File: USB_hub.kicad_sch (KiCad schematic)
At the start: 0 parts

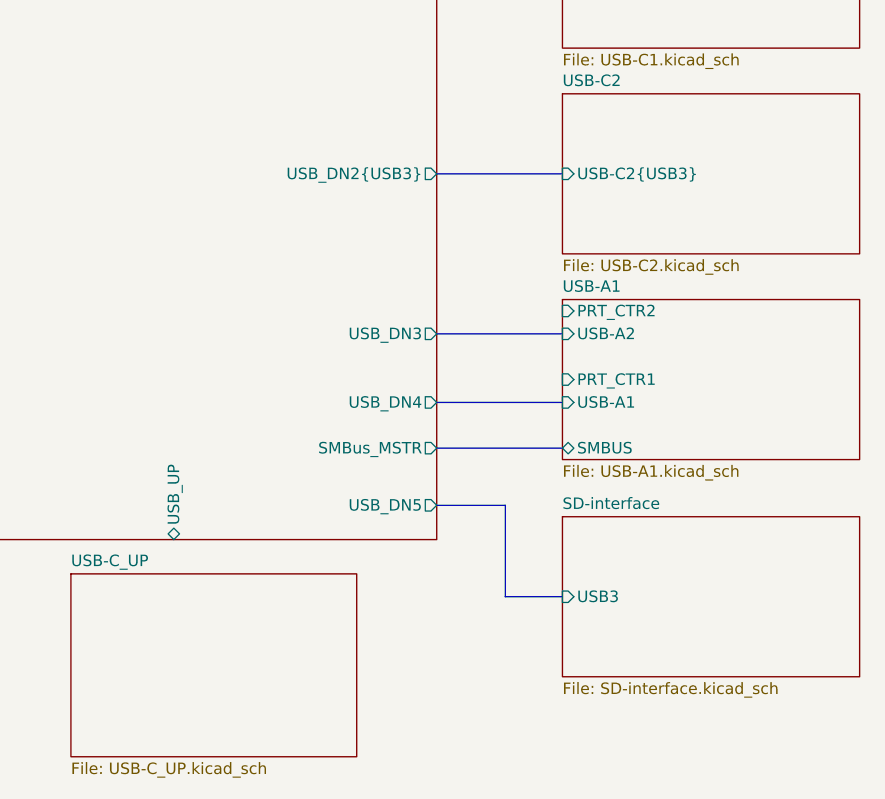
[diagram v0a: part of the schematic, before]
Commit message: labels naming fixes, USB Type E connector added
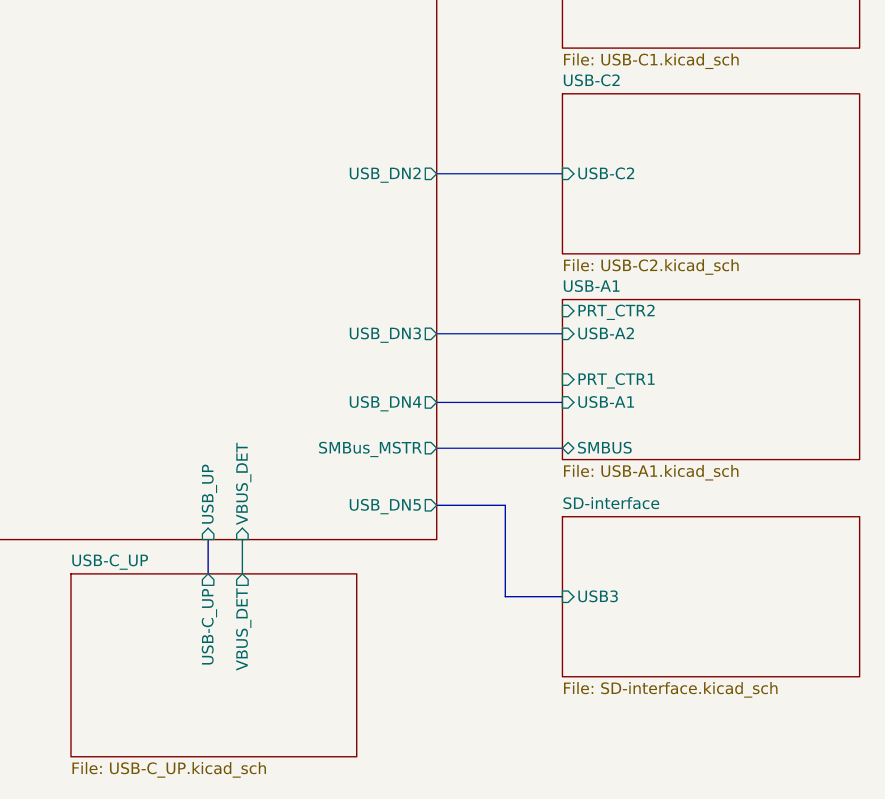
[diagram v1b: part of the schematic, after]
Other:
- sheet USB-C2 ports: added USB-C2; removed USB-C2{USB3}
- sheet USB-C_UP ports: added USB-C_UP, VBUS_DET; removed none
- sheet USB7206C ports: added USB_DN2, VBUS_DET; removed USB_DN2{USB3}
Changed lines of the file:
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@@
+		)
+	)
+	(wire
+		(pts
+			(xy 248.92 92.71) (xy 248.92 96.52)
+		)
+		(stroke
+			(width 0)
+			(type default)
 		)
 	)
@@
 		(pts
 			(xy 270.51 82.55) (xy 284.48 82.55)
+		)
+		(stroke
+			(width 0)
+			(type default)
+		)
+	)
+	(bus
+		(pts
+			(xy 245.11 92.71) (xy 245.11 96.52)
 		)
 		(stroke
@@
 			)
 		)
-		(pin "USB-C2{USB3}" input
+		(pin "USB-C2" input
 			(at 284.48 52.07 180)
 			(effects
@@
 			)
 		)
+		(pin "VBUS_DET" output
+			(at 248.92 96.52 90)
+			(effects
+				(font
+					(size 1.27 1.27)
+				)
+				(justify right)
+			)
+		)
+		(pin "USB-C_UP" output
+			(at 245.11 96.52 90)
+			(effects
+				(font
+					(size 1.27 1.27)
+				)
+				(justify right)
+			)
+		)
 		(instances
 			(project "USB_hub"
@@
 			)
 		)
-		(pin "USB_UP" bidirectional
-			(at 241.3 92.71 270)
-			(effects
-				(font
-					(size 1.27 1.27)
-				)
-				(justify left)
-			)
-		)
 		(pin "USB_DN3" output
 			(at 270.51 69.85 0)
@@
 			)
 		)
-		(pin "USB_DN2{USB3}" output
+		(pin "USB_UP" input
+			(at 245.11 92.71 270)
+			(effects
+				(font
+					(size 1.27 1.27)
+				)
+				(justify left)
+			)
+		)
+		(pin "USB_DN2" output
 			(at 270.51 52.07 0)
 			(effects
@@
 			)
 		)
+		(pin "VBUS_DET" input
+			(at 248.92 92.71 270)
+			(effects
+				(font
+					(size 1.27 1.27)
+				)
+				(justify left)
+			)
+		)

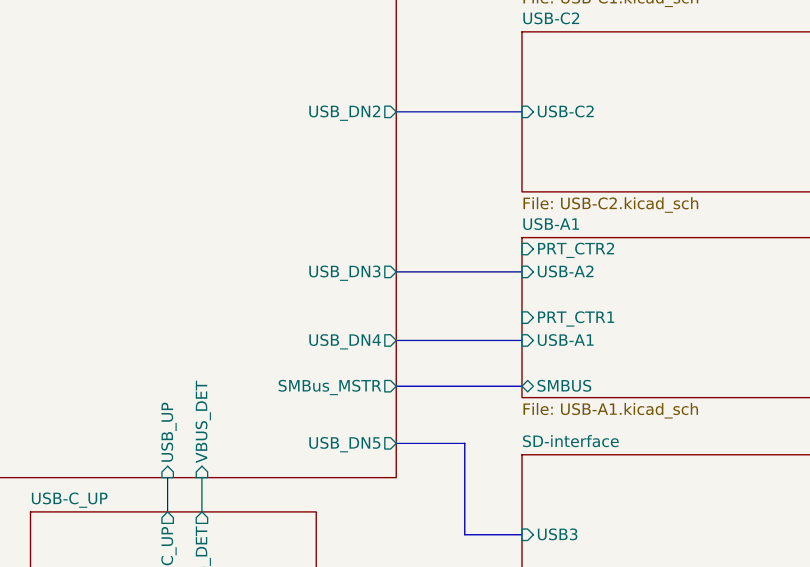
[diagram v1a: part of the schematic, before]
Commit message: Port Power Control added to USB7206C schematics
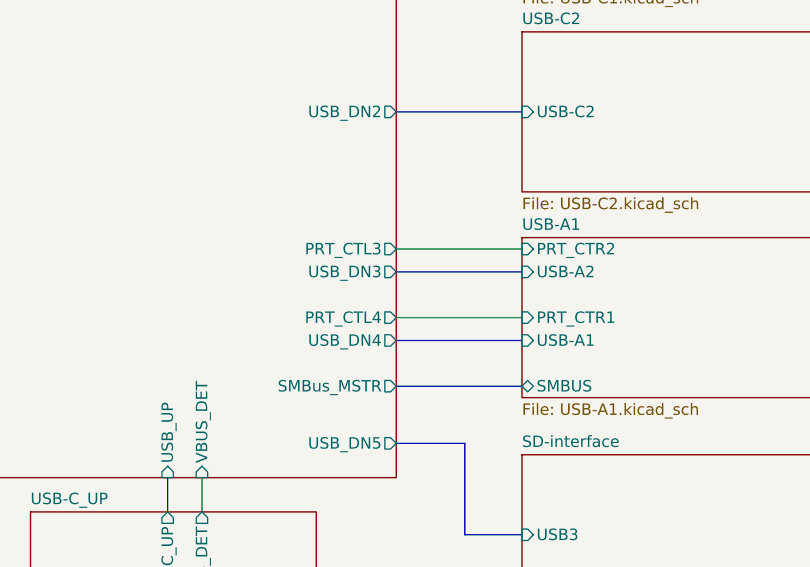
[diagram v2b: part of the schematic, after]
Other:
- sheet USB7206C ports: added PRT_CTL3, PRT_CTL4; removed none
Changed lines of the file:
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@@
+		)
+	)
+	(wire
+		(pts
+			(xy 270.51 74.93) (xy 284.48 74.93)
+		)
+		(stroke
+			(width 0)
+			(type default)
 		)
 	)
@@
 		(pts
 			(xy 270.51 29.21) (xy 284.48 29.21)
+		)
+		(stroke
+			(width 0)
+			(type default)
+		)
+	)
+	(wire
+		(pts
+			(xy 270.51 67.31) (xy 284.48 67.31)
 		)
 		(stroke
@@
 			)
 		)
+		(pin "PRT_CTL4" output
+			(at 270.51 74.93 0)
+			(effects
+				(font
+					(size 1.27 1.27)
+				)
+				(justify right)
+			)
+		)
+		(pin "PRT_CTL3" output
+			(at 270.51 67.31 0)
+			(effects
+				(font
+					(size 1.27 1.27)
+				)
+				(justify right)
+			)
+		)

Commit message: TPS25762 EEPROM connector added
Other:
- title: (none) -> USB Hub
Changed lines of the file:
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@@
 	(generator_version "9.0")
 	(paper "A3")
+	(title_block
+		(title "USB Hub")
+	)
 	(text "these connections may change for better routing "
 		(exclude_from_sim no)

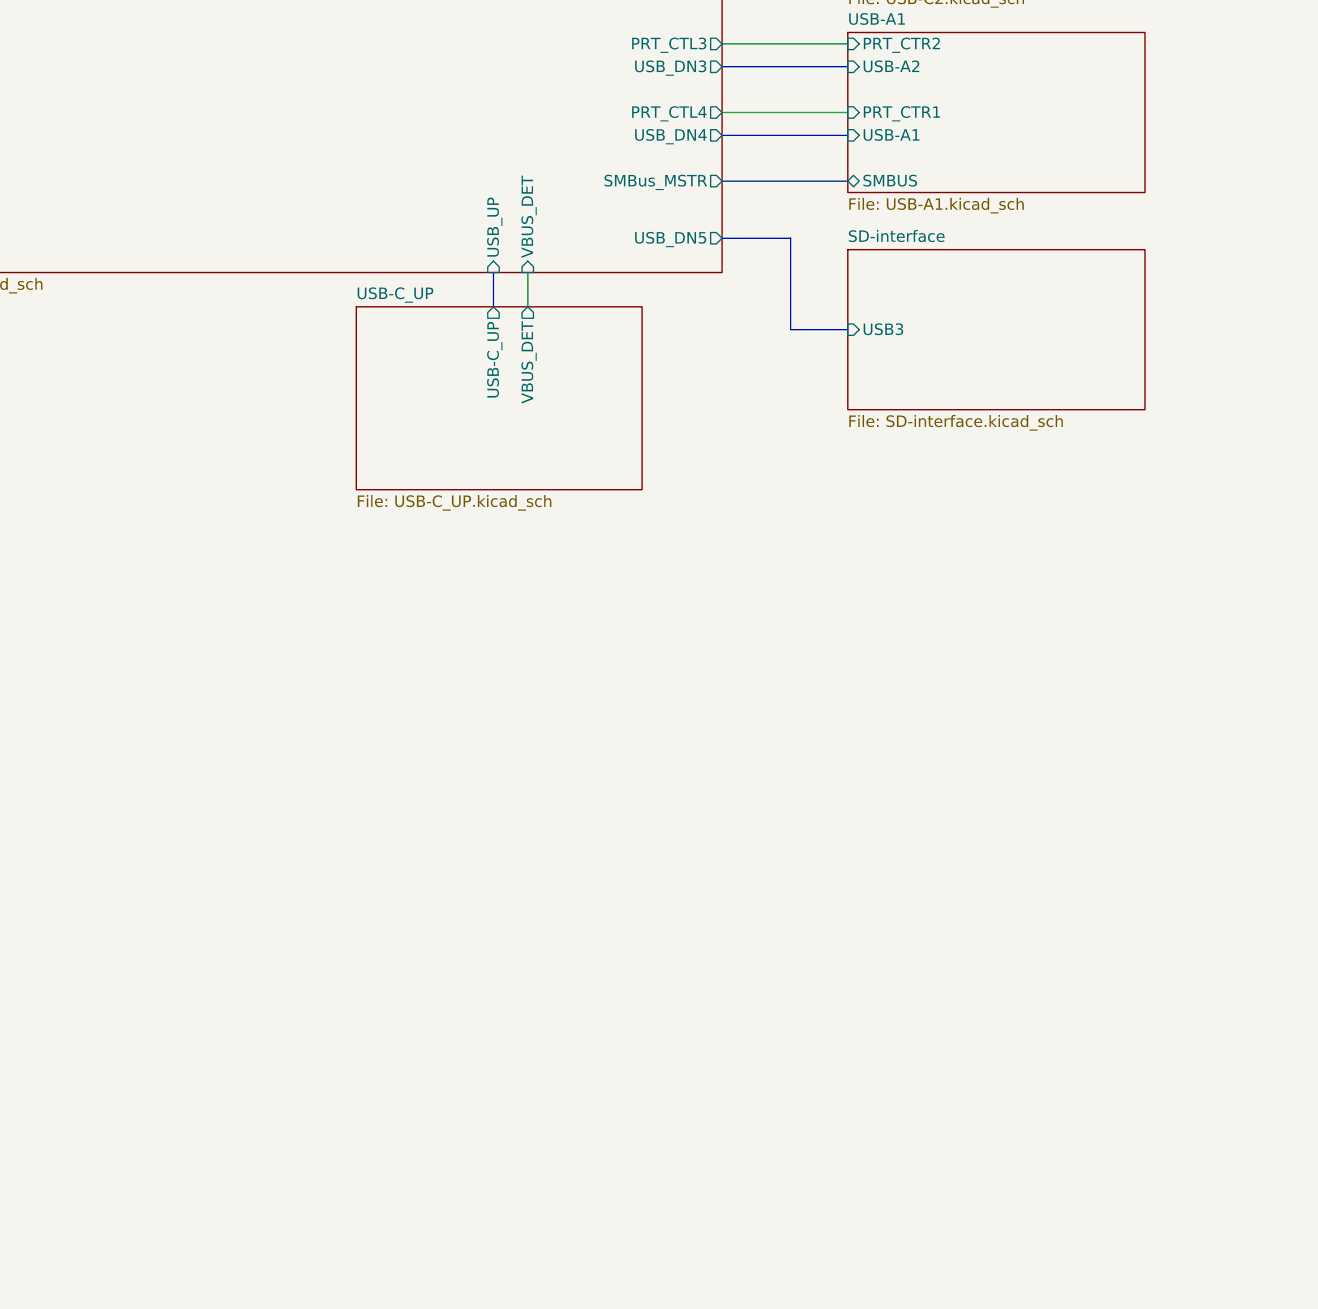
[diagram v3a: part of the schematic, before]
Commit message: MCP19035 changed to MP8795
TPS7A4701xRGW to AP7361C-33E
Led Indicator added
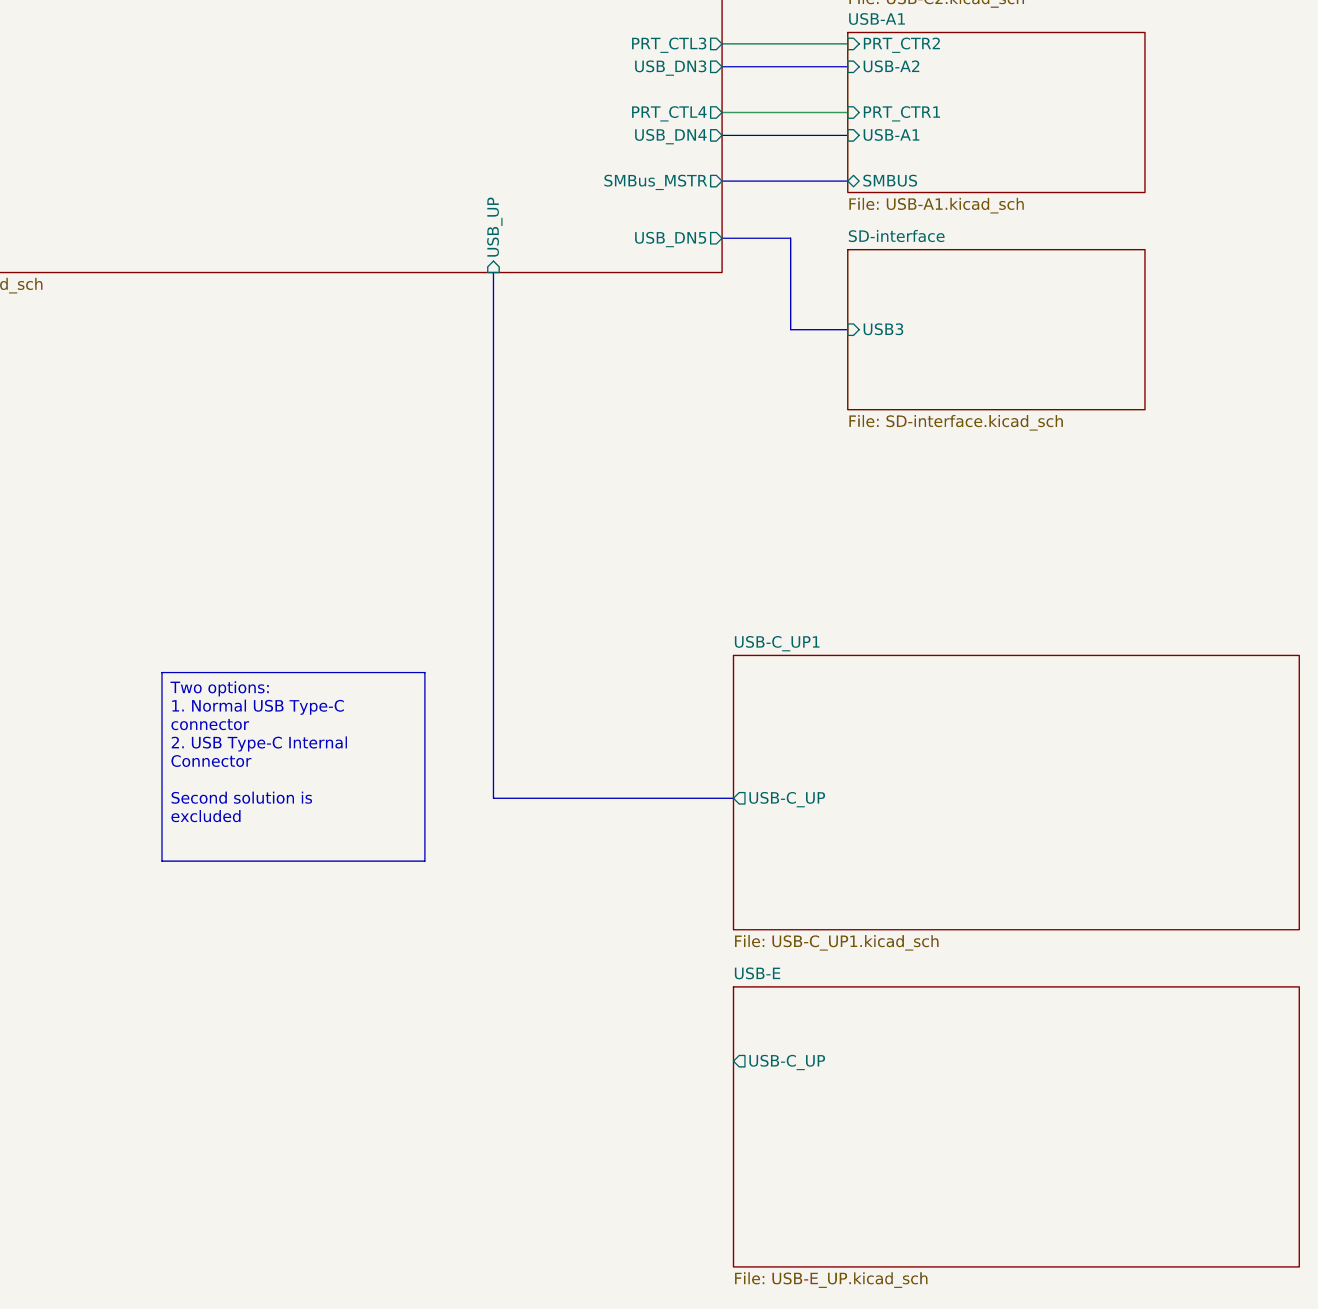
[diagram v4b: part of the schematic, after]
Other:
- removed sheet USB-C_UP
- added sheet USB-C_UP1 (USB-C_UP1.kicad_sch)
- added sheet USB-E (USB-E_UP.kicad_sch)
- sheet USB7206C ports: added none; removed VBUS_DET

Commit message: I2C Addresses added to scheme
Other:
- sheet USB-A1 ports: added PRT_EN1, PRT_EN2; removed PRT_CTR1, PRT_CTR2, SMBUS
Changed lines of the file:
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@@
-			)
-		)
-		(pin "SMBUS" bidirectional
-			(at 284.48 82.55 180)
-			(effects
-				(font
-					(size 1.27 1.27)
-				)
-				(justify left)
 			)
 		)
@@
 			)
 		)
-		(pin "PRT_CTR2" input
+		(pin "USB-A2" input
+			(at 284.48 69.85 180)
+			(effects
+				(font
+					(size 1.27 1.27)
+				)
+				(justify left)
+			)
+		)
+		(pin "PRT_EN2" input
 			(at 284.48 67.31 180)
 			(effects
@@
 			)
 		)
-		(pin "PRT_CTR1" input
+		(pin "PRT_EN1" input
 			(at 284.48 74.93 180)
 			(effects
 				(font
-					(size 1.27 1.27)
-				)
-				(justify left)
-			)
-		)
-		(pin "USB-A2" input
-			(at 284.48 69.85 180)
-			(effects
-				(font

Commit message: Net class for USB SS signals created and applied on schematic
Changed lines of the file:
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@@
 	(bus
 		(pts
-			(xy 270.51 52.07) (xy 284.48 52.07)
-		)
-		(stroke
-			(width 0)
-			(type default)
-		)
-	)
-	(bus
-		(pts
-			(xy 278.13 88.9) (xy 278.13 99.06)
+			(xy 278.13 52.07) (xy 278.13 69.85)
 		)
 		(stroke
@@
 		(pts
 			(xy 270.51 74.93) (xy 284.48 74.93)
-		)
-		(stroke
-			(width 0)
-			(type default)
-		)
-	)
-	(bus
-		(pts
-			(xy 270.51 69.85) (xy 284.48 69.85)
-		)
-		(stroke
-			(width 0)
-			(type default)
-		)
-	)
-	(bus
-		(pts
-			(xy 270.51 29.21) (xy 284.48 29.21)
 		)
 		(stroke
@@
 	(bus
 		(pts
-			(xy 270.51 82.55) (xy 284.48 82.55)
+			(xy 270.51 52.07) (xy 278.13 52.07)
+		)
+		(stroke
+			(width 0)
+			(type default)
+		)
+	)
+	(bus
+		(pts
+			(xy 284.48 52.07) (xy 280.67 52.07)
+		)
+		(stroke
+			(width 0)
+			(type default)
+		)
+	)
+	(bus
+		(pts
+			(xy 278.13 69.85) (xy 284.48 69.85)
+		)
+		(stroke
+			(width 0)
+			(type default)
+		)
+	)
+	(bus
+		(pts
+			(xy 280.67 52.07) (xy 280.67 88.9)
 		)
 		(stroke
@@
 	(bus
 		(pts
-			(xy 278.13 99.06) (xy 284.48 99.06)
+			(xy 270.51 88.9) (xy 280.67 88.9)
 		)
 		(stroke
@@
 	(bus
 		(pts
-			(xy 270.51 77.47) (xy 284.48 77.47)
+			(xy 276.86 69.85) (xy 276.86 77.47)
 		)
 		(stroke
@@
 	(bus
 		(pts
-			(xy 270.51 88.9) (xy 278.13 88.9)
+			(xy 275.59 77.47) (xy 275.59 99.06)
 		)
 		(stroke
+			(width 0)
+			(type default)
+		)
+	)
+	(bus
+		(pts
+			(xy 270.51 69.85) (xy 276.86 69.85)
+		)
+		(stroke
+			(width 0)
+			(type default)
+		)
+	)
+	(bus
+		(pts
+			(xy 270.51 77.47) (xy 275.59 77.47)
+		)
+		(stroke
+			(width 0)
+			(type default)
+		)
+	)
+	(bus
+		(pts
+			(xy 275.59 99.06) (xy 284.48 99.06)
+		)
+		(stroke
+			(width 0)
+			(type default)
+		)
+	)
+	(bus
+		(pts
+			(xy 270.51 29.21) (xy 284.48 29.21)
+		)
+		(stroke
+			(width 0)
+			(type default)
+		)
+	)
+	(bus
+		(pts
+			(xy 276.86 77.47) (xy 284.48 77.47)
+		)
+		(stroke

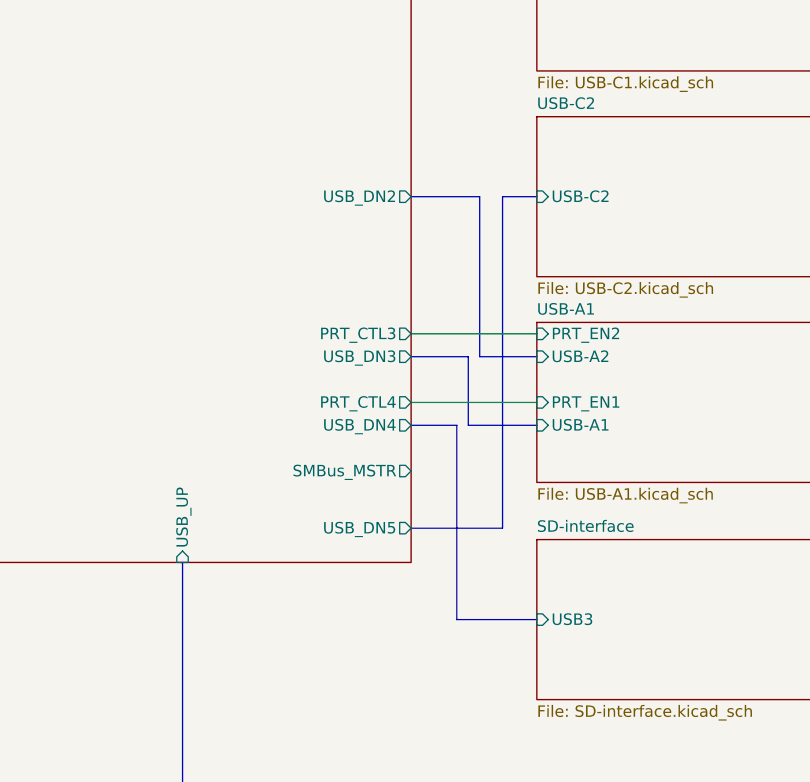
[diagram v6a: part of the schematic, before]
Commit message: Added lcsc part number for most of components, fixes for better routing
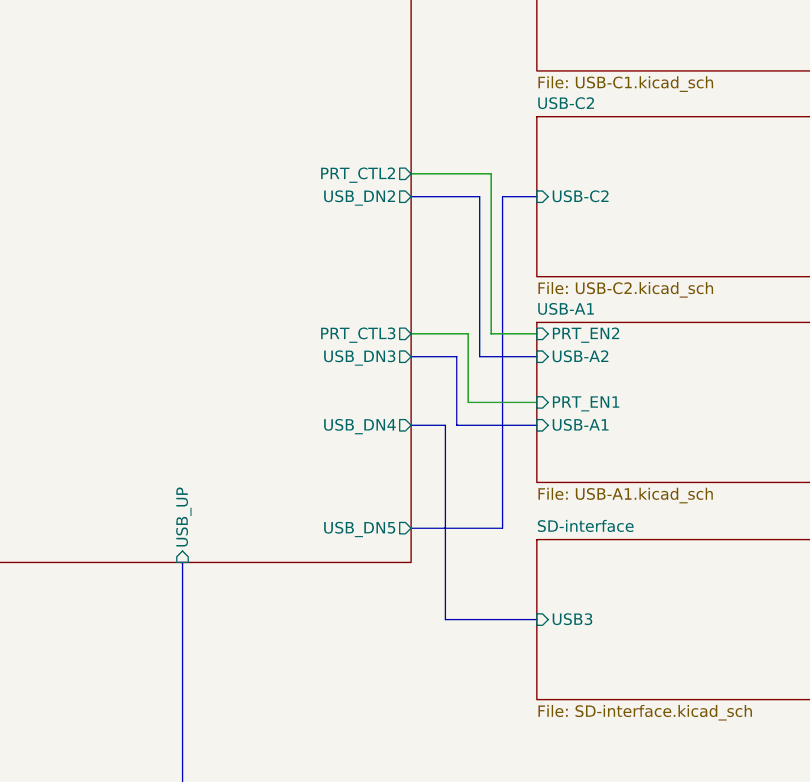
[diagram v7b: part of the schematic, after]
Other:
- sheet USB7206C ports: added PRT_CTL2; removed PRT_CTL4, SMBus_MSTR
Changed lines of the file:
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@@
-		)
-	)
-	(wire
-		(pts
-			(xy 270.51 74.93) (xy 284.48 74.93)
-		)
-		(stroke
-			(width 0)
-			(type default)
-		)
-	)
-	(wire
-		(pts
-			(xy 270.51 67.31) (xy 284.48 67.31)
-		)
-		(stroke
-			(width 0)
-			(type default)
 		)
 	)
@@
 		)
 	)
+	(wire
+		(pts
+			(xy 270.51 49.53) (xy 279.4 49.53)
+		)
+		(stroke
+			(width 0)
+			(type default)
+		)
+	)
+	(wire
+		(pts
+			(xy 284.48 74.93) (xy 276.86 74.93)
+		)
+		(stroke
+			(width 0)
+			(type default)
+		)
+	)
 	(bus
 		(pts
@@
 		)
 	)
-	(bus
-		(pts
-			(xy 276.86 69.85) (xy 276.86 77.47)
-		)
-		(stroke
-			(width 0)
-			(type default)
-		)
-	)
-	(bus
-		(pts
-			(xy 275.59 77.47) (xy 275.59 99.06)
-		)
-		(stroke
-			(width 0)
-			(type default)
-		)
-	)
-	(bus
-		(pts
-			(xy 270.51 69.85) (xy 276.86 69.85)
-		)
-		(stroke
-			(width 0)
-			(type default)
-		)
-	)
-	(bus
-		(pts
-			(xy 270.51 77.47) (xy 275.59 77.47)
-		)
-		(stroke
-			(width 0)
-			(type default)
-		)
-	)
-	(bus
-		(pts
-			(xy 275.59 99.06) (xy 284.48 99.06)
+	(wire
+		(pts
+			(xy 279.4 67.31) (xy 284.48 67.31)
+		)
+		(stroke
+			(width 0)
+			(type default)
+		)
+	)
+	(bus
+		(pts
+			(xy 275.59 69.85) (xy 275.59 77.47)
+		)
+		(stroke
+			(width 0)
+			(type default)
+		)
+	)
+	(bus
+		(pts
+			(xy 274.32 77.47) (xy 274.32 99.06)
+		)
+		(stroke
+			(width 0)
+			(type default)
+		)
+	)
+	(bus
+		(pts
+			(xy 270.51 69.85) (xy 275.59 69.85)
+		)
+		(stroke
+			(width 0)
+			(type default)
+		)
+	)
+	(bus
+		(pts
+			(xy 270.51 77.47) (xy 274.32 77.47)
+		)
+		(stroke
+			(width 0)
+			(type default)
+		)
+	)
+	(wire
+		(pts
+			(xy 270.51 67.31) (xy 276.86 67.31)
+		)
+		(stroke
+			(width 0)
+			(type default)
+		)
+	)
+	(wire
+		(pts
+			(xy 276.86 74.93) (xy 276.86 67.31)
+		)
+		(stroke
+			(width 0)
+			(type default)
+		)
+	)
+	(wire
+		(pts
+			(xy 279.4 49.53) (xy 279.4 67.31)
+		)
+		(stroke
+			(width 0)
+			(type default)
+		)
+	)
+	(bus
+		(pts
+			(xy 274.32 99.06) (xy 284.48 99.06)
 		)
 		(stroke
@@
 	(bus
 		(pts
-			(xy 276.86 77.47) (xy 284.48 77.47)
+			(xy 275.59 77.47) (xy 284.48 77.47)
 		)
 		(stroke
@@
 			)
 		)
-		(pin "SMBus_MSTR" output
-			(at 270.51 82.55 0)
-			(effects
-				(font
-					(size 1.27 1.27)
-				)
-				(justify right)
-			)
-		)
 		(pin "USB_UP" input
 			(at 245.11 92.71 270)
@@
 			)
 		)
-		(pin "PRT_CTL4" output
-			(at 270.51 74.93 0)
-			(effects
-				(font
-					(size 1.27 1.27)
-				)
-				(justify right)
-			)
-		)
 		(pin "PRT_CTL3" output
 			(at 270.51 67.31 0)
 			(effects
 				(font
+					(size 1.27 1.27)
+				)
+				(justify right)
+			)
+		)
+		(pin "PRT_CTL2" output
+			(at 270.51 49.53 0)
+			(effects
+				(font
